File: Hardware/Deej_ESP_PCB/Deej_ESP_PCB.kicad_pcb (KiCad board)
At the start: 2 copper layers, 206 x 183.5 mm, 149 parts, among them J1 USB_C_Receptacle_USB2.0_16P, J2 UART Header, P1 10K, P2 10K, P3 10K, P4 10K, P5 10K, P6 10K, SW1 SW_Push, SW2 SW_Push, SW3 SW_Push, SW4 SW_Push, SW5 SW_Push, SW6 SW_Push, SW7 Reset, U1 10K, U10 1.3" 128x64 OLED, U11 1.3" 128x64 OLED, U2 10K, U3 ECMF02-2AMX6, U4 SN74HCS126DR, U5 LMS1585ACS-3.3/NOPB, U6 SN74HCS126DR, U7 ESP32-S3-MINI-1U, U8 1.3" 128x64 OLED, U9 1.3" 128x64 OLED

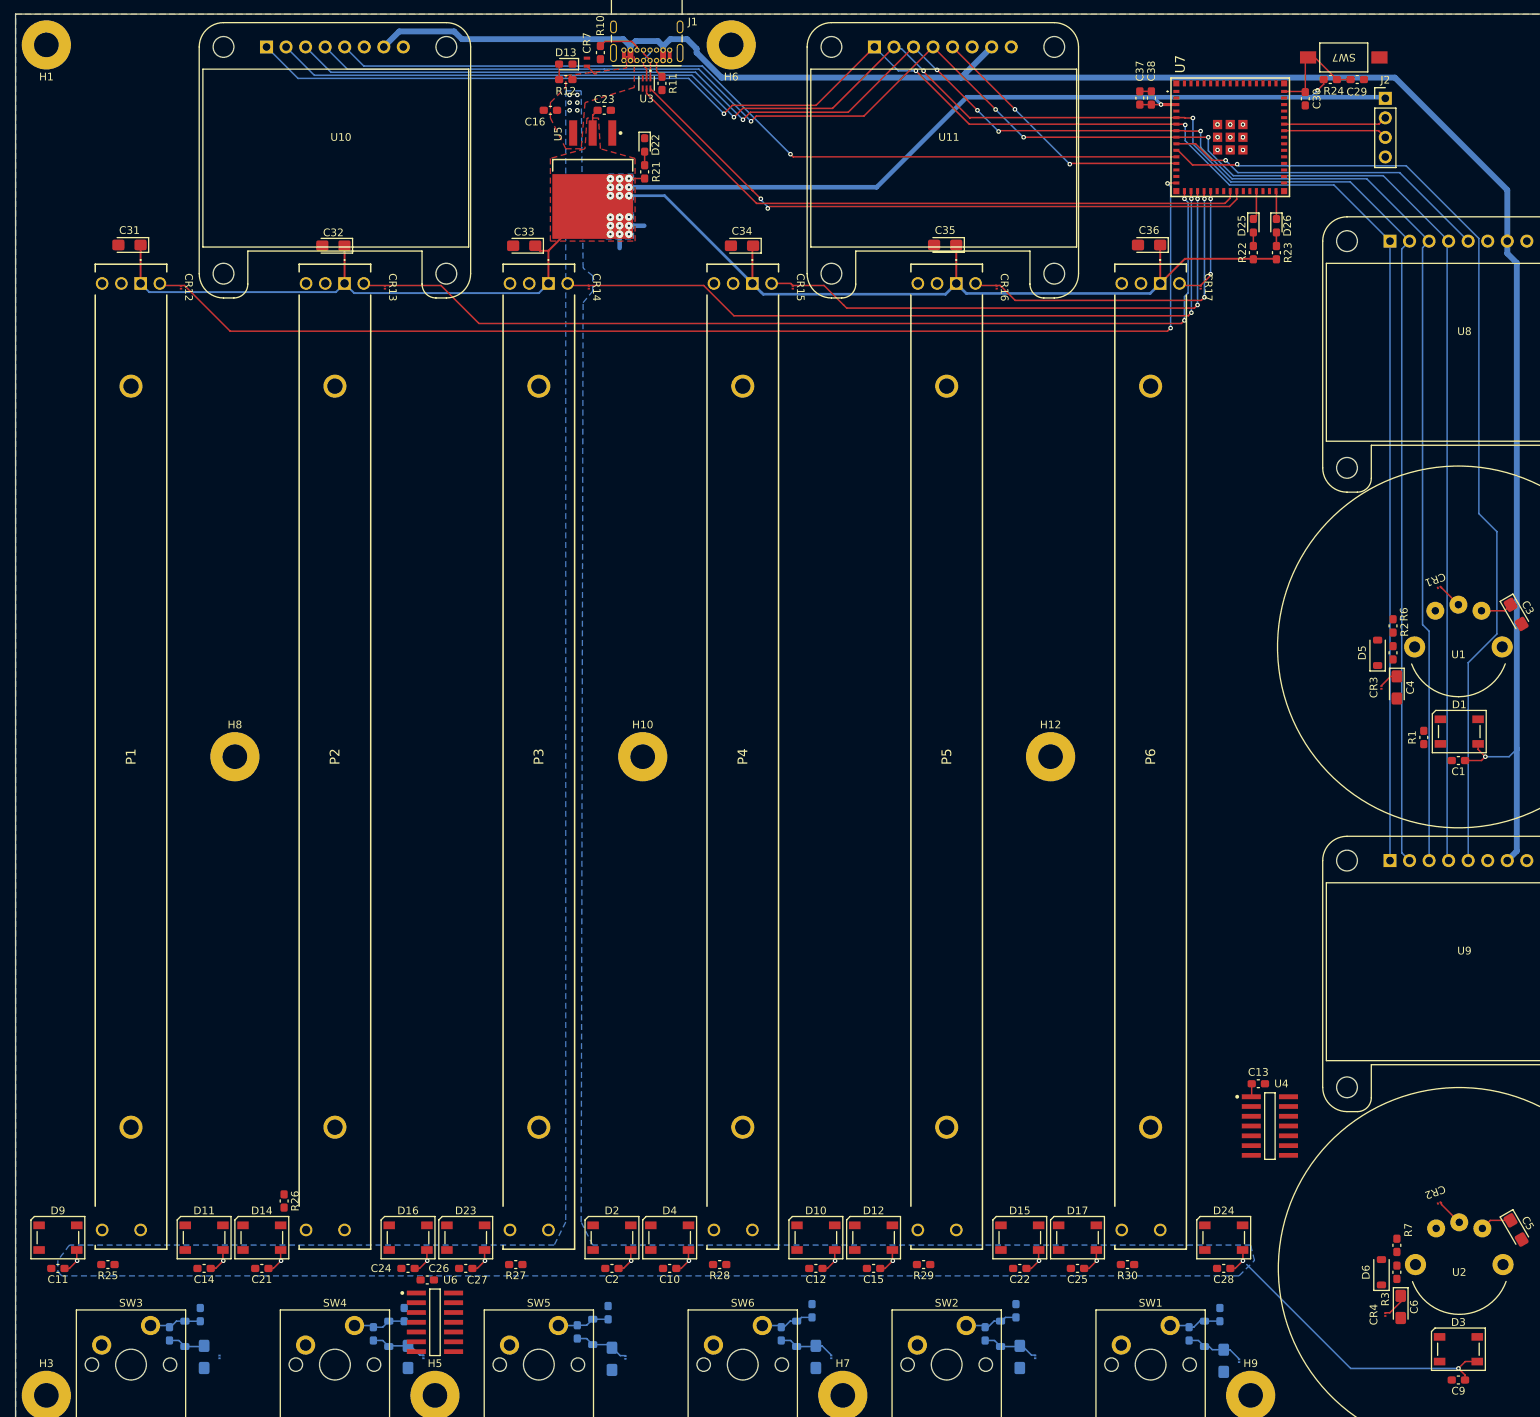
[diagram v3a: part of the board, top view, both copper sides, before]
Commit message: More Power Routing and NEO Pixel LED Routing
- Added more +3.3V voltage routing
- Added some signaling for the NEO Pixel LEDs

TODO: Other LED traces and analog dials
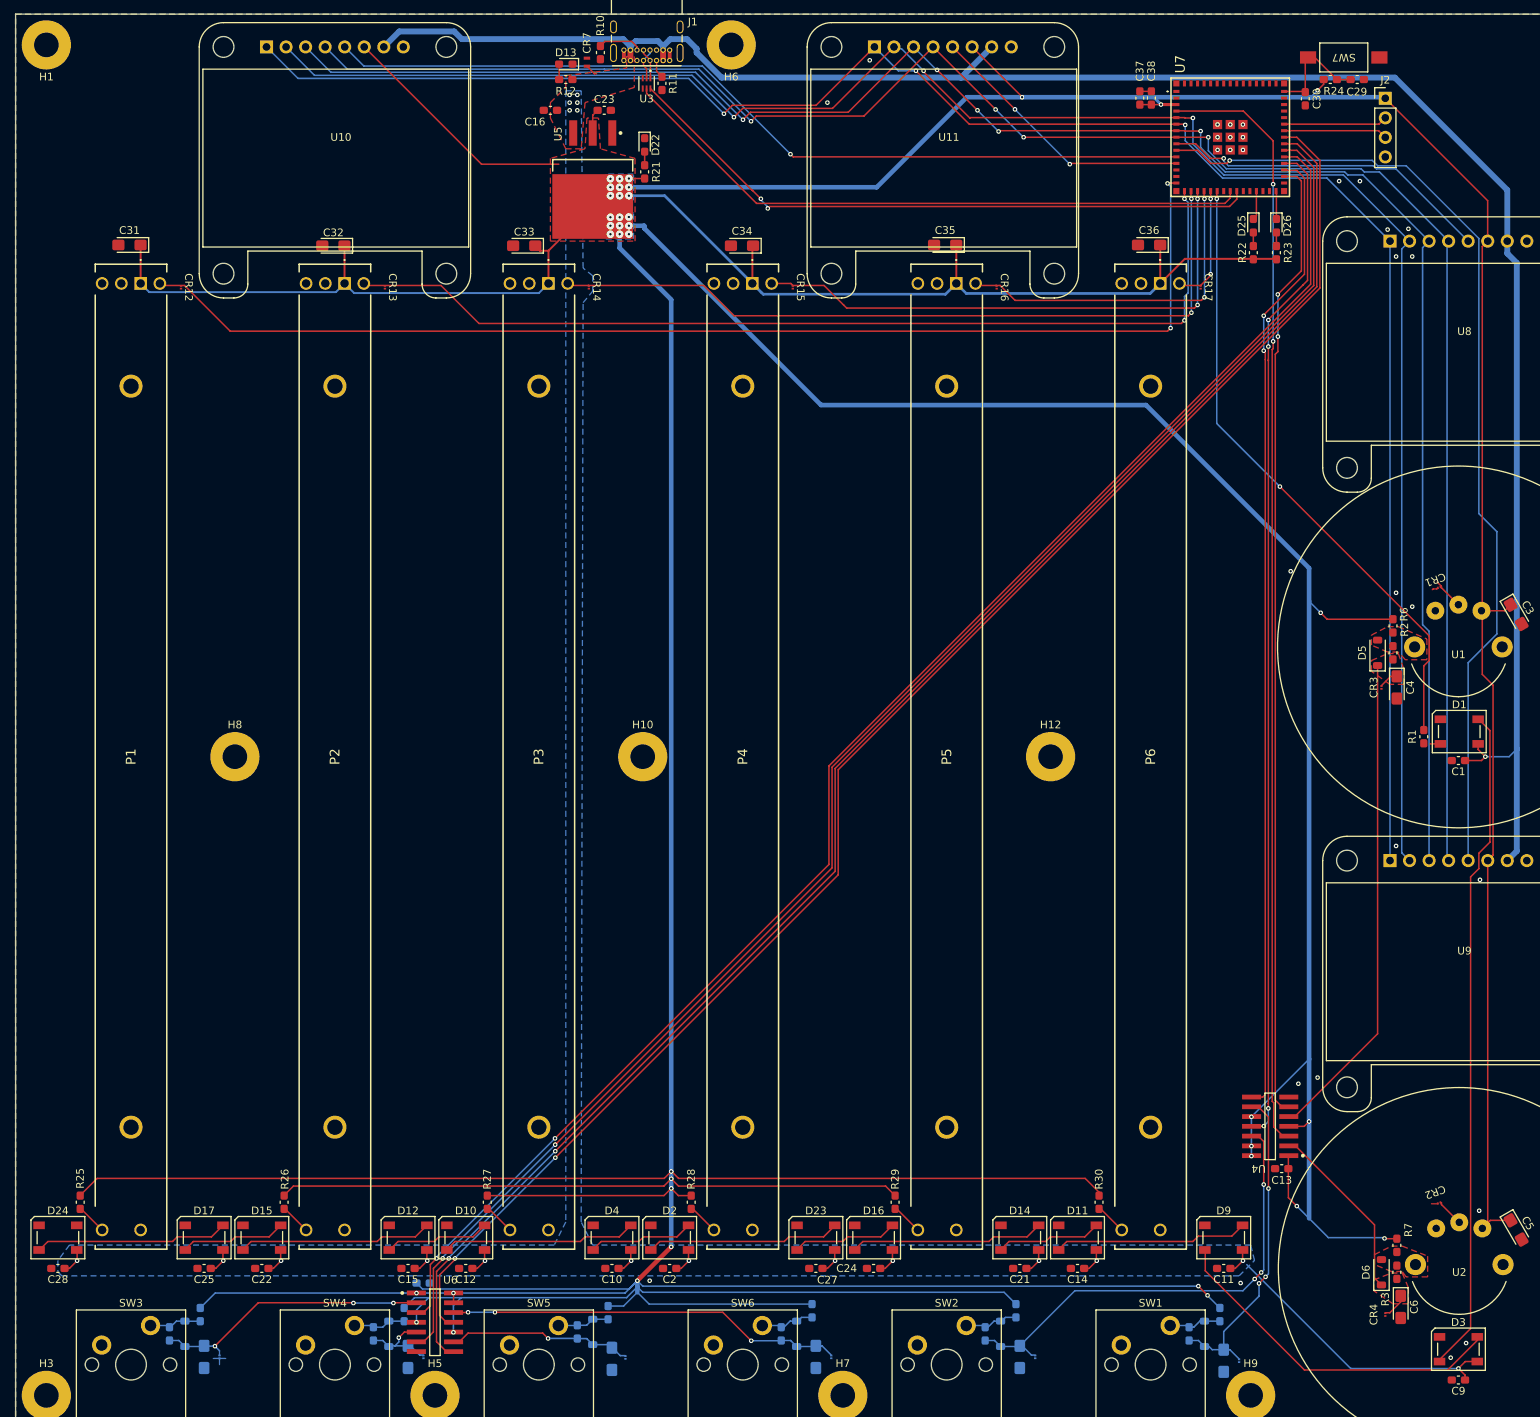
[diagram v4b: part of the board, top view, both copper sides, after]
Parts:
- C26: moved to B.Cu
- moved C11 151.5 mm to (254.0, 221.5)
- moved C28 151.5 mm to (102.5, 221.5)
- moved D24 151.5 mm to (102.5, 217.5)
- moved D9 151.5 mm to (254.0, 217.5)
- moved C14 113.5 mm to (235.0, 221.5)
- moved C25 113.5 mm to (121.5, 221.5)
- moved D11 113.5 mm to (235.0, 217.5)
- moved D17 113.5 mm to (121.5, 217.5)
- moved C21 98.5 mm to (227.5, 221.5)
- moved C22 98.5 mm to (129.0, 221.5)
- moved D14 98.5 mm to (227.5, 217.5)
- moved D15 98.5 mm to (129.0, 217.5)
- moved C15 60.5 mm to (148.0, 221.5)
- moved C24 60.5 mm to (208.5, 221.5)
- moved D12 60.5 mm to (148.0, 217.5)
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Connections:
- U4 pad 12: Net-(D8-A) -> Net-(D8-K)
- U4 pad 2: Net-(D5-A) -> Net-(D6-K)
- U4 pad 5: Net-(D6-A) -> Net-(D5-K)
- U4 pad 9: Net-(D7-A) -> Net-(D7-K)
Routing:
- net +3.3V: track 324.0 -> 1427.3 mm, vias 20 -> 39
- net /MuteSW_6: track 0.00 -> 208.6 mm, vias 0 -> 2
- net /MuteSW_5: track 0.00 -> 206.4 mm, vias 0 -> 2
- net /MuteSW_7: track 0.00 -> 205.6 mm, vias 0 -> 2
- net /MuteSW_4: track 0.00 -> 201.3 mm, vias 0 -> 2
- net /MuteSW_0: track 0.00 -> 144.8 mm, vias 0 -> 2
- net /MuteSW_3: track 0.00 -> 131.3 mm, vias 0 -> 4
- net /MuteSW_2: track 0.00 -> 126.3 mm, vias 0 -> 2
- net /MuteSW_1: track 0.00 -> 125.5 mm, vias 0 -> 2
- net Net-(D1-DO): track 0.00 -> 86.8 mm
- net /NEOLED_0: track 0.00 -> 81.8 mm, vias 0 -> 2
- net Net-(D5-K): track 2.50 -> 66.4 mm
- net Net-(D8-K): track 7.36 -> 61.7 mm, vias 0 -> 3
- net Net-(D3-DO): track 0.00 -> 45.3 mm
- net Net-(D21-K): track 7.36 -> 51.5 mm, vias 0 -> 3
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- added copper zone on F.Cu, net Net-(D5-A)
- added copper zone on F.Cu, net Net-(D5-K)
- added copper zone on F.Cu, net Net-(D6-A)
- added copper zone on F.Cu, net Net-(D6-K)

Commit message: Finished Running Traces, On to DRC Fixes
- I believe I finished running the traces to get everything connected
  KiCAD shows one more air wire but that seems like a visual isses since
  I can confirm it is connected.
- Next I will be starting on fixing the 94 DRC ERRORs. A lot of them
  seems really simple on first glance so I'm not worried about those but
  there are a few errors involving clearances and manufacturing minimums.
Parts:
- moved C33 0.70 mm to (163.8, 88.6)
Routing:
- net /Analog_1: track 3.53 -> 164.5 mm, vias 0 -> 6
- net /MuteLED_1: track 0.00 -> 158.0 mm, vias 0 -> 4
- net /MuteLED_2: track 0.00 -> 132.7 mm, vias 0 -> 2
- net /MuteLED_3: track 0.00 -> 106.9 mm, vias 0 -> 2
- net /Analog_0: track 4.09 -> 90.8 mm, vias 0 -> 4
- net /MuteLED_4: track 0.00 -> 82.0 mm, vias 0 -> 2
- net /MuteLED_5: track 0.00 -> 56.4 mm, vias 0 -> 2
- net /MuteLED_6: track 0.00 -> 36.3 mm, vias 0 -> 2
- net GND: track 8.18 -> 4.20 mm
- net /Analog_2: track 154.2 -> 155.5 mm
- net /Analog_3: track 126.2 -> 127.2 mm
- net +5V: track 345.0 -> 345.7 mm
- net /Analog_4: track 98.9 -> 99.6 mm
- net +3.3V: track 1427.3 -> 1426.8 mm
- net Net-(D18-K): track 36.2 -> 36.1 mm, vias 3 -> 1
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
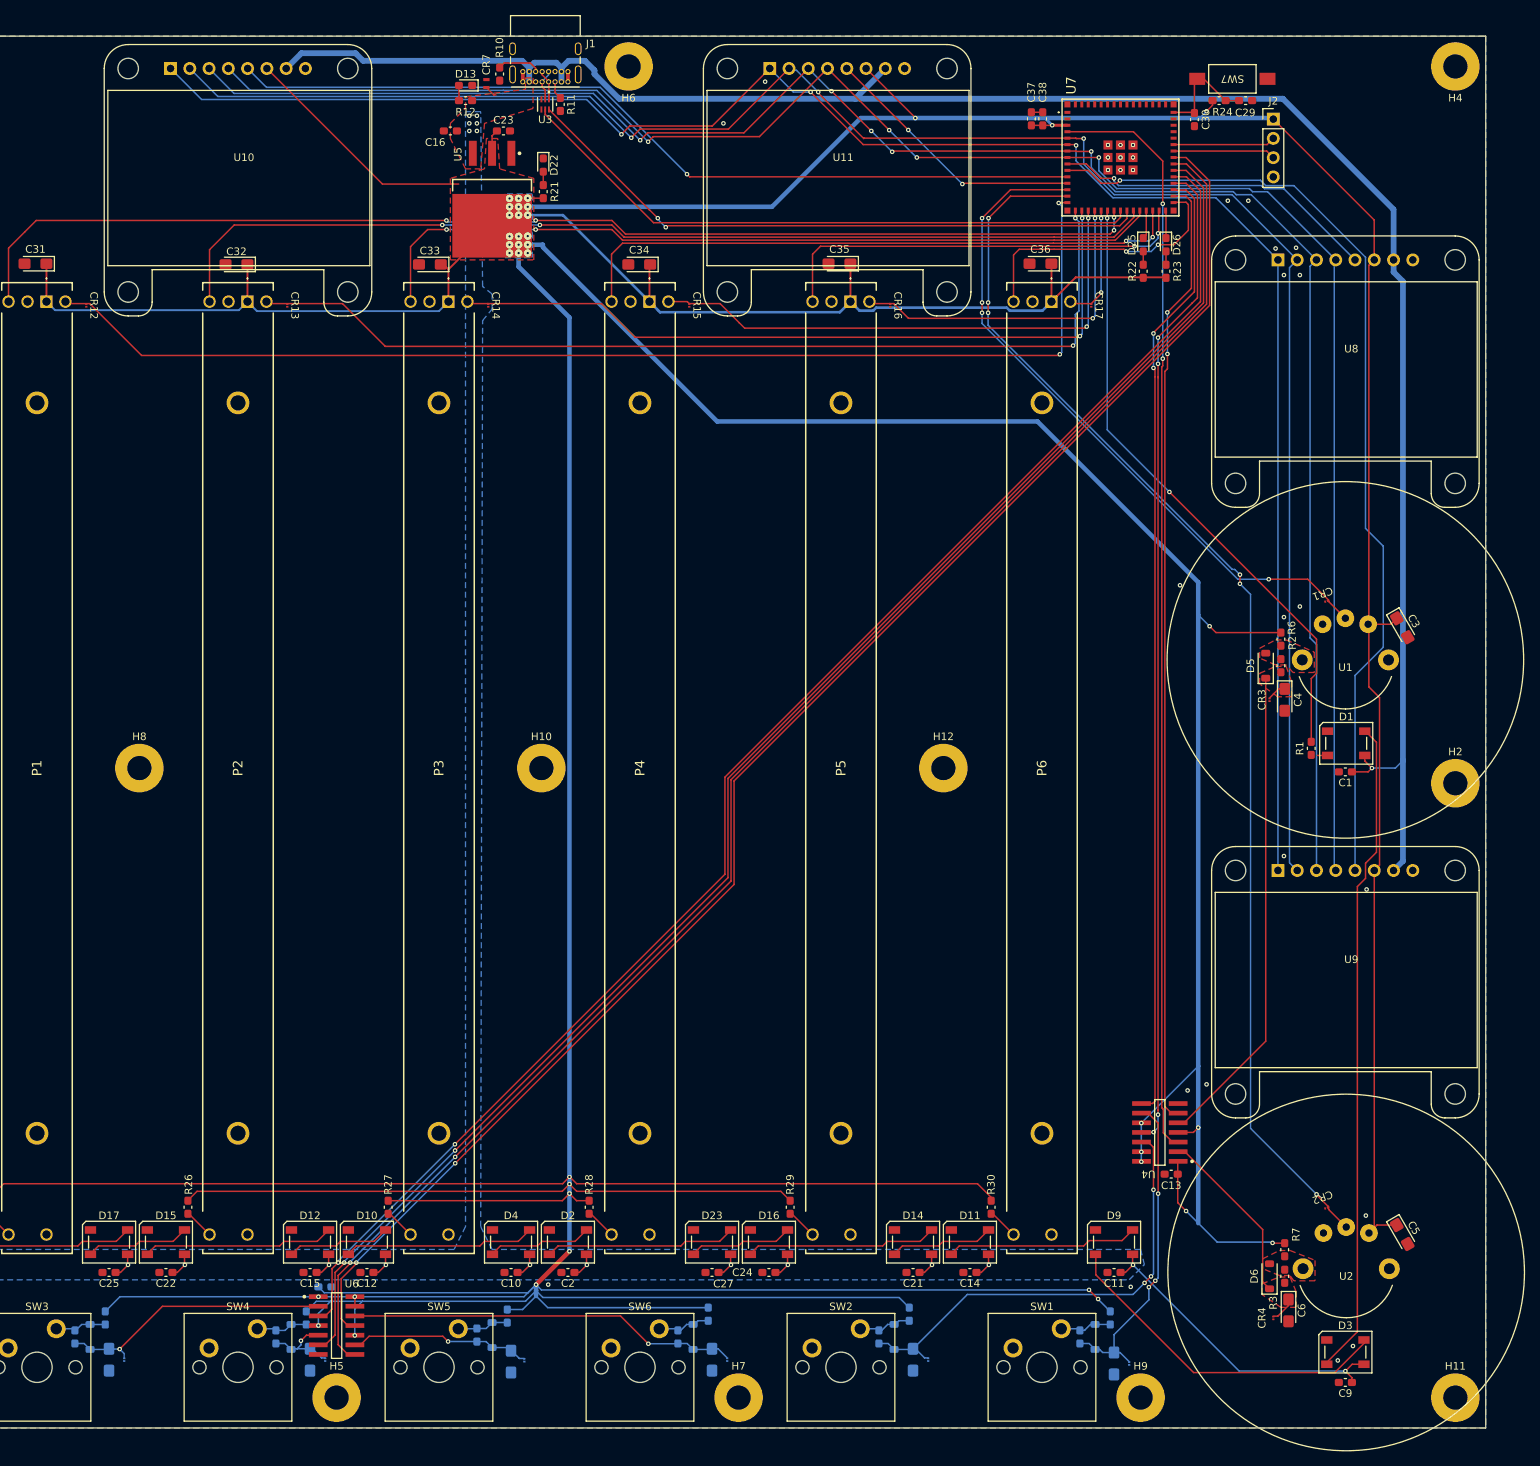
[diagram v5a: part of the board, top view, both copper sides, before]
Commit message: -Trace routing 'done' ... until I find another issue -Fixing DRC errors and warnings
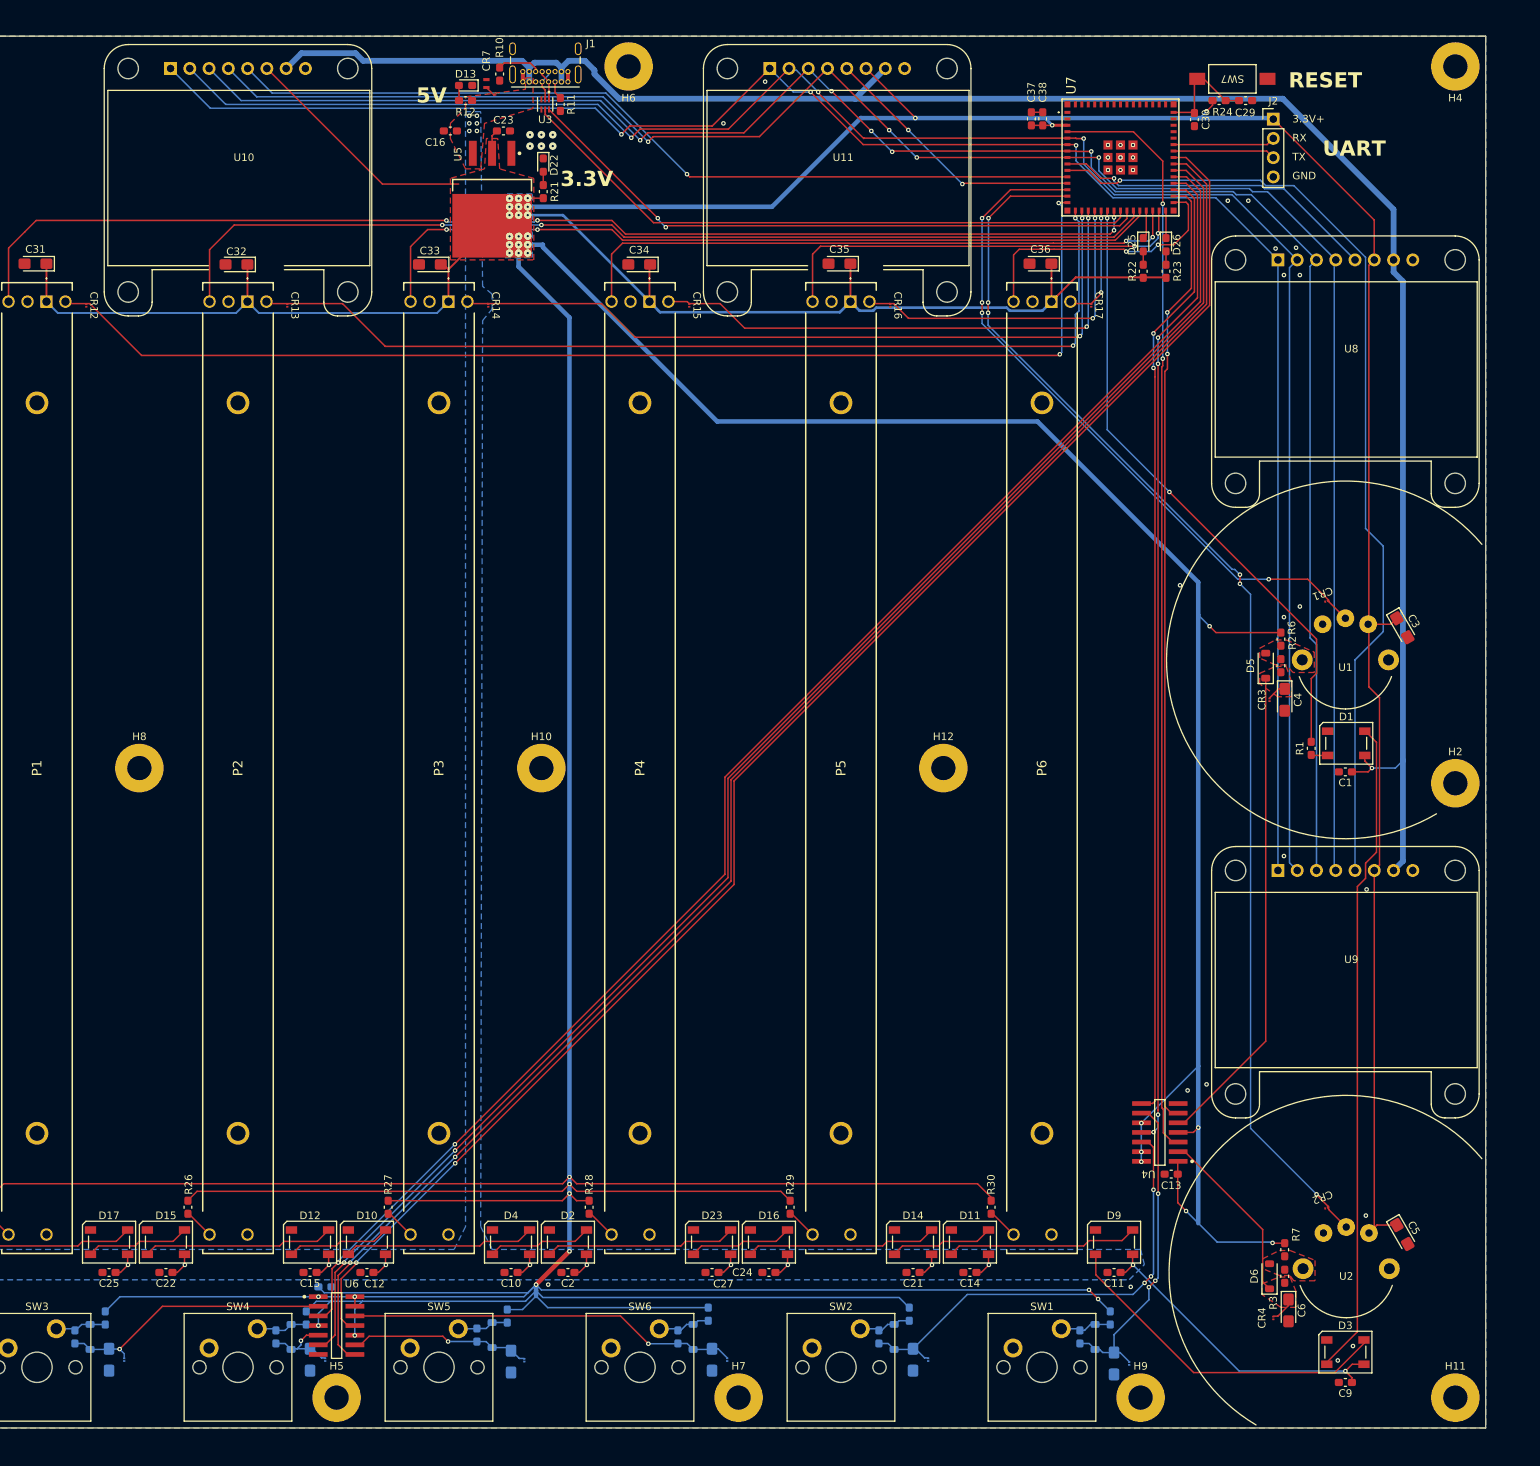
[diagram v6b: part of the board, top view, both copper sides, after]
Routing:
- net GND: track 4.20 -> 6.90 mm, vias 29 -> 35
- net Net-(D1-DIN): track 1.41 -> 2.24 mm
- net +3.3V: track 1426.8 -> 1427.3 mm
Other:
- board text added: "3.3V"
- board text added: "3.3V+"
- board text added: "5V"
- board text added: "GND"
- board text added: "RESET"
- board text added: "RX"
- board text added: "TX"
- board text added: "UART"
